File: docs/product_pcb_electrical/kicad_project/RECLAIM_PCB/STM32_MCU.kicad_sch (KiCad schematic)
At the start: 16 parts, among them U4 STM32F405RGT6, Y1 8MHz

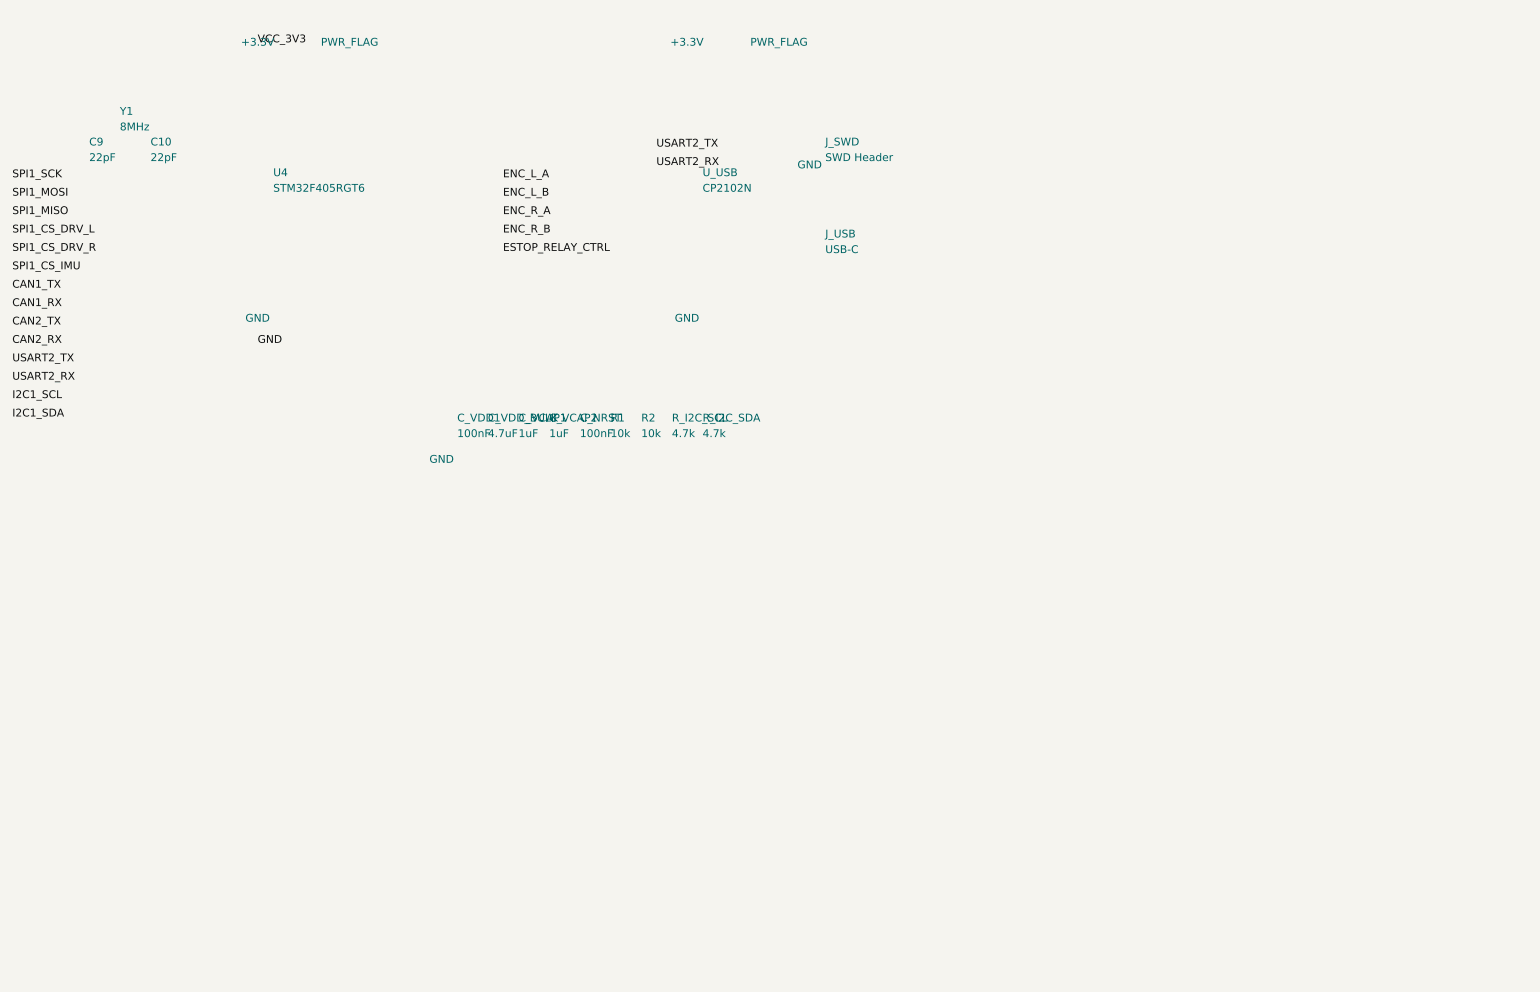
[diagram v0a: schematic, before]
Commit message: Add prototype schematic + tighten product layout to A3
Product: All 4 sub-sheets resized A2/A1→A3, components repositioned
into tight logical groups, duplicate K1/Q1 removed.

Prototype: New KiCad project with 3 hierarchical sheets
(Power, Teensy/Motor Control, Peripherals/Sensors), BOM, and
netlist reflecting as-built wiring: MD13C R3 + BTS7960 asymmetric
drivers, DC disconnect, 6-way fuse block, XINGYHENG servo buck.

Co-Authored-By: Claude Opus 4.6 <noreply@anthropic.com>
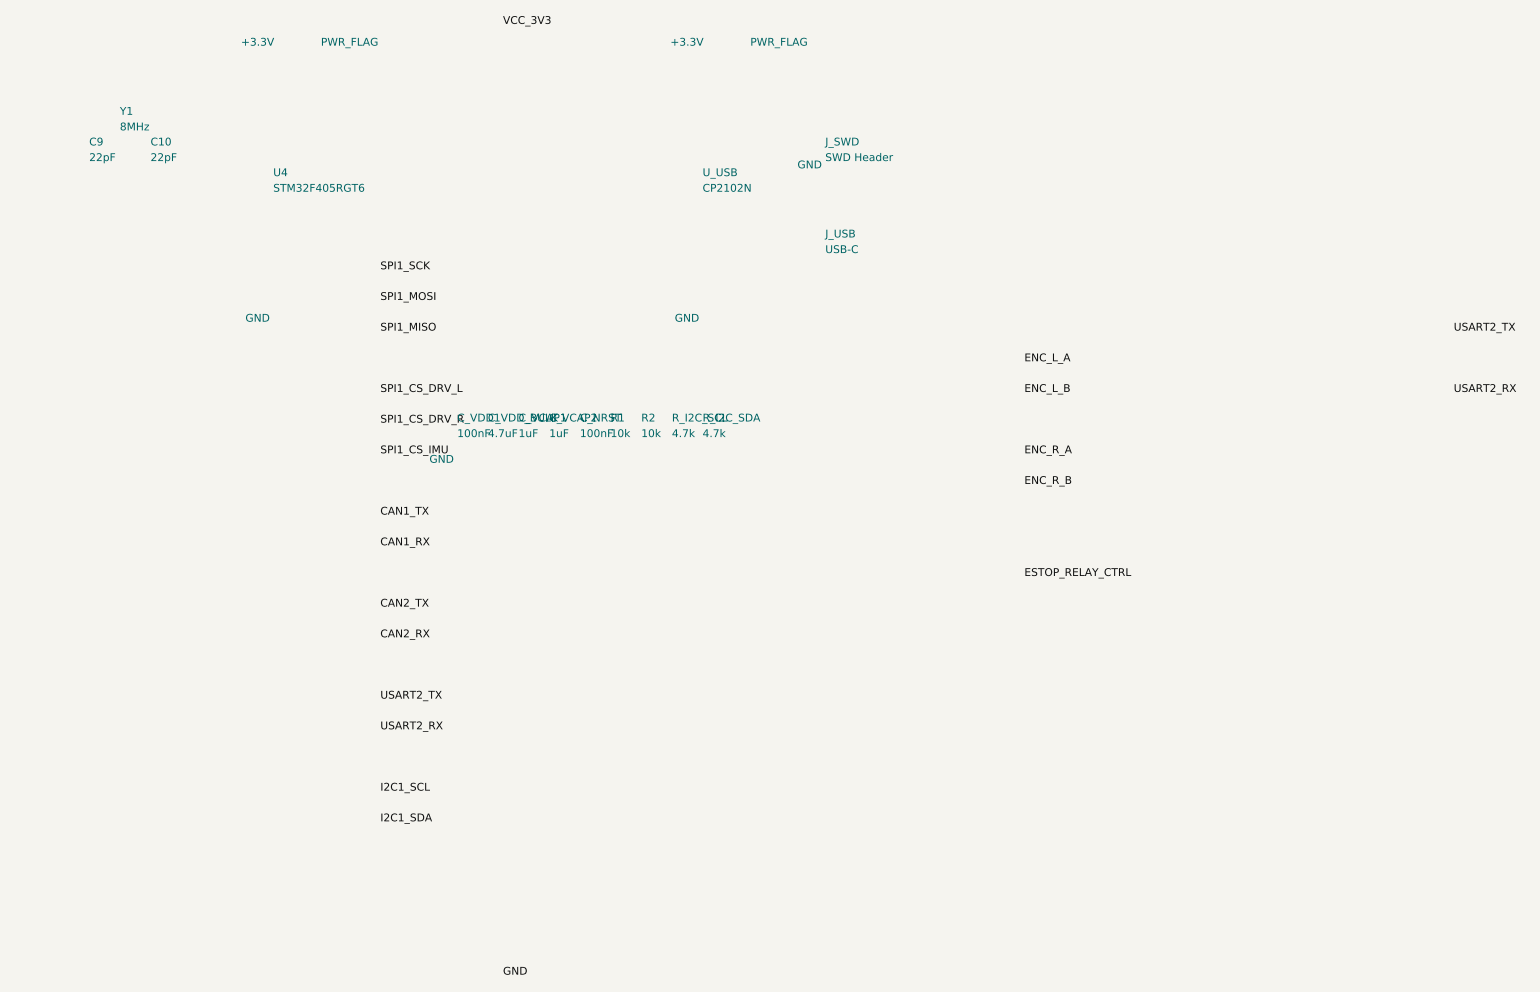
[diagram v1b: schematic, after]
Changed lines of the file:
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@@
 	(generator "eeschema")
 	(generator_version "10.0")
-	(paper "A1")
+	(paper "A3")
 	(title_block
 		(title "RECLAIM Product PCB - STM32F405 MCU")
@@
 	(symbol
 		(lib_id "MCU_ST_STM32F4:STM32F405RGTx")
-		(at 80 60 0)
+		(at 150 100 0)
 		(unit 1)
 		(body_style 1)
@@
 	(symbol
 		(lib_id "Interface_USB:CP2102N-Axx-xQFN24")
-		(at 150 60 0)
+		(at 295 90 0)
 		(unit 1)
 		(body_style 1)
@@
 	(symbol
 		(lib_id "Device:Crystal")
-		(at 55 50 0)
+		(at 70 85 0)
 		(unit 1)
 		(body_style 1)
@@
 	(symbol
 		(lib_id "Device:C")
-		(at 50 55 0)
+		(at 60 98 0)
 		(unit 1)
 		(body_style 1)
@@
 	(symbol
 		(lib_id "Device:C")
-		(at 60 55 0)
+		(at 80 98 0)
 		(unit 1)
 		(body_style 1)
@@
 	(symbol
 		(lib_id "Device:C")
-		(at 110 100 0)
+		(at 120 215 0)
 		(unit 1)
 		(body_style 1)
@@
 	(symbol
 		(lib_id "Device:C")
-		(at 115 100 0)
+		(at 132 215 0)
 		(unit 1)
 		(body_style 1)
@@
 	(symbol
 		(lib_id "Device:C")
-		(at 120 100 0)
+		(at 144 215 0)
 		(unit 1)
 		(body_style 1)
@@
 	(symbol
 		(lib_id "Device:C")
-		(at 125 100 0)
+		(at 156 215 0)
 		(unit 1)
 		(body_style 1)
@@
 	(symbol
 		(lib_id "Device:C")
-		(at 130 100 0)
+		(at 168 215 0)
 		(unit 1)
 		(body_style 1)
@@
 	(symbol
 		(lib_id "Device:R")
-		(at 135 100 0)
+		(at 230 80 0)
 		(unit 1)
 		(body_style 1)
@@
 	(symbol
 		(lib_id "Device:R")
-		(at 140 100 0)
+		(at 230 95 0)
 		(unit 1)
 		(body_style 1)
@@
 	(symbol
 		(lib_id "Device:R")
-		(at 145 100 0)
+		(at 230 115 0)
 		(unit 1)
 		(body_style 1)
@@
 	(symbol
 		(lib_id "Device:R")
-		(at 150 100 0)
+		(at 230 130 0)
 		(unit 1)
 		(body_style 1)
@@
 	(symbol
 		(lib_id "Connector_Generic:Conn_01x04")
-		(at 170 55 0)
+		(at 365 70 0)
 		(unit 1)
 		(body_style 1)
@@
 	(symbol
 		(lib_id "Connector_Generic:Conn_01x04")
-		(at 170 70 0)
+		(at 365 110 0)
 		(unit 1)
 		(body_style 1)
@@
 	(symbol
 		(lib_id "power:+3V3")
-		(at 80 40 0)
+		(at 120 30 0)
 		(unit 1)
 		(body_style 1)
@@
 	(symbol
 		(lib_id "power:+3V3")
-		(at 150 40 0)
+		(at 290 30 0)
 		(unit 1)
 		(body_style 1)
@@
 	(symbol
 		(lib_id "power:GND")
-		(at 80 85 0)
+		(at 120 195 0)
 		(unit 1)
 		(body_style 1)
@@
 	(symbol
 		(lib_id "power:GND")
-		(at 150 85 0)
+		(at 290 155 0)
 		(unit 1)
 		(body_style 1)
@@
 	(symbol
 		(lib_id "power:GND")
-		(at 110 108 0)
+		(at 155 230 0)
 		(unit 1)
 		(body_style 1)
@@
 	(symbol
 		(lib_id "power:GND")
-		(at 170 60 0)
+		(at 365 120 0)
 		(unit 1)
 		(body_style 1)
@@
 	(symbol
 		(lib_id "power:PWR_FLAG")
-		(at 95 40 0)
+		(at 130 30 0)
 		(unit 1)
 		(body_style 1)
@@
 	(symbol
 		(lib_id "power:PWR_FLAG")
-		(at 165 40 0)
+		(at 300 30 0)
 		(unit 1)
 		(body_style 1)
@@
 	)
 	(label "VCC_3V3"
-		(at 80 38 0)
+		(at 120 35 0)
 		(fields_autoplaced yes)
 		(effects
@@
 	)
 	(label "GND"
-		(at 80 87 0)
+		(at 120 190 0)
 		(fields_autoplaced yes)
 		(effects
@@
 	)
 	(label "SPI1_SCK"
-		(at 40 60 0)
+		(at 100 75 180)
 		(fields_autoplaced yes)
 		(effects
@@
 	)
 	(label "SPI1_MOSI"
-		(at 40 63 0)
+		(at 100 80 180)
 		(fields_autoplaced yes)
 		(effects
@@
 	)
 	(label "SPI1_MISO"
-		(at 40 66 0)
+		(at 100 85 180)
 		(fields_autoplaced yes)
 		(effects
@@
 	)
 	(label "SPI1_CS_DRV_L"
-		(at 40 69 0)
+		(at 100 95 180)
 		(fields_autoplaced yes)
 		(effects
@@
 	)
 	(label "SPI1_CS_DRV_R"
-		(at 40 72 0)
+		(at 100 100 180)
 		(fields_autoplaced yes)
 		(effects
@@
 	)
 	(label "SPI1_CS_IMU"
-		(at 40 75 0)
+		(at 100 105 180)
 		(fields_autoplaced yes)
 		(effects
@@
 	)
 	(label "CAN1_TX"
-		(at 40 78 0)
+		(at 100 115 180)
 		(fields_autoplaced yes)
 		(effects
@@
 	)
 	(label "CAN1_RX"
-		(at 40 81 0)
+		(at 100 120 180)
 		(fields_autoplaced yes)
 		(effects
@@
 	)
 	(label "CAN2_TX"
-		(at 40 84 0)
+		(at 100 130 180)
 		(fields_autoplaced yes)
 		(effects
@@
 	)
 	(label "CAN2_RX"
-		(at 40 87 0)
+		(at 100 135 180)
 		(fields_autoplaced yes)
 		(effects
@@
 	)
 	(label "USART2_TX"
-		(at 40 90 0)
+		(at 100 145 180)
 		(fields_autoplaced yes)
 		(effects
@@
 	)
 	(label "USART2_RX"
-		(at 40 93 0)
+		(at 100 150 180)
 		(fields_autoplaced yes)
 		(effects
@@
 	)
 	(label "I2C1_SCL"
-		(at 40 96 0)
+		(at 100 160 180)
 		(fields_autoplaced yes)
 		(effects
@@
 	)
 	(label "I2C1_SDA"
-		(at 40 99 0)
+		(at 100 165 180)
 		(fields_autoplaced yes)
 		(effects
@@
 	)
 	(label "ENC_L_A"
-		(at 120 60 0)
+		(at 205 90 0)
 		(fields_autoplaced yes)
 		(effects
@@
 	)
 	(label "ENC_L_B"
-		(at 120 63 0)
+		(at 205 95 0)
 		(fields_autoplaced yes)
 		(effects
@@
 	)
 	(label "ENC_R_A"
-		(at 120 66 0)
+		(at 205 105 0)
 		(fields_autoplaced yes)
 		(effects
@@
 	)
 	(label "ENC_R_B"
-		(at 120 69 0)
+		(at 205 110 0)
 		(fields_autoplaced yes)
 		(effects
@@
 	)
 	(label "ESTOP_RELAY_CTRL"
-		(at 120 72 0)
+		(at 205 125 0)
 		(fields_autoplaced yes)
 		(effects
@@
 	)
 	(label "USART2_TX"
-		(at 145 55 0)
+		(at 275 85 180)
 		(fields_autoplaced yes)
 		(effects
@@
 	)
 	(label "USART2_RX"
-		(at 145 58 0)
-		(fields_autoplaced yes)
-		(effects
+		(at 275 95 180)
+		(fields_autoplaced yes)
+		(effects
